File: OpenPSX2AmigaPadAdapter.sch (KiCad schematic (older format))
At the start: 47 parts, among them J1 TO_PSX_PAD, J2 DB9_F, J3 CONN_FTDI, J4 CONN_ICSP, J99 OSHW_LOGO, Q1 BSS138, Q2 BSS138, Q3 BSS138, Q4 BSS138, Q5 BSS138, U1 ATmega328P-AU, U2 TC1185-3.3V, U3 AD5242, Y1 16M, Y2 16M

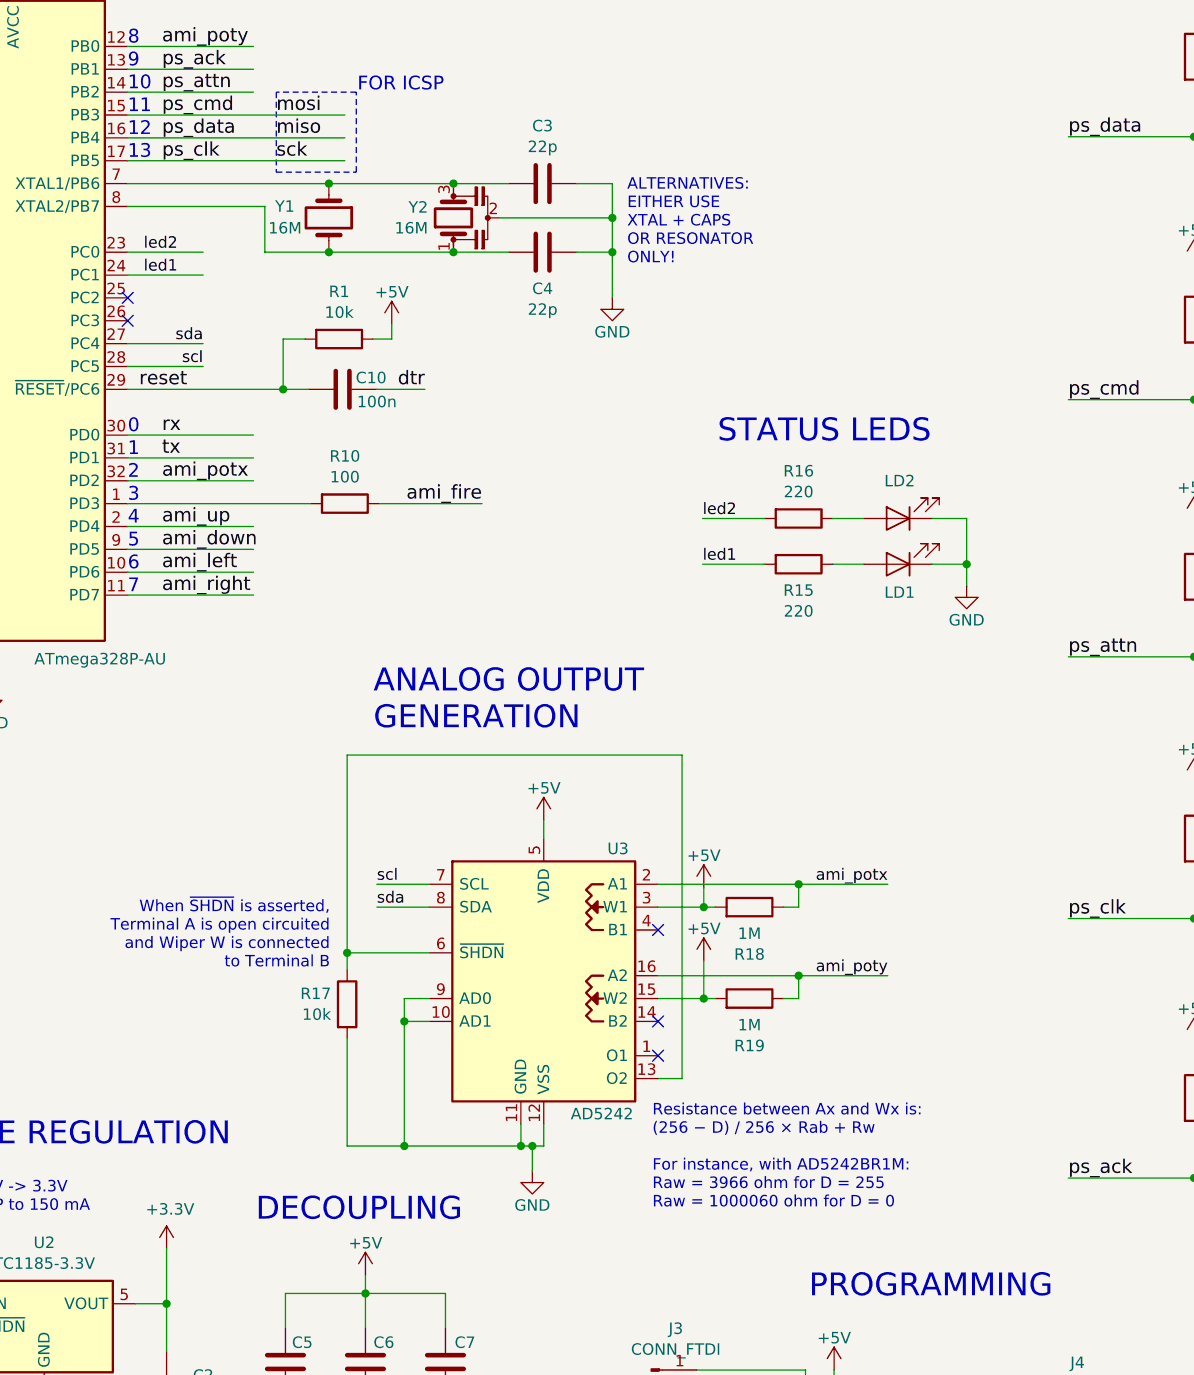
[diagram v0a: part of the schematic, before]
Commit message: PCB modifications for analog support are complete
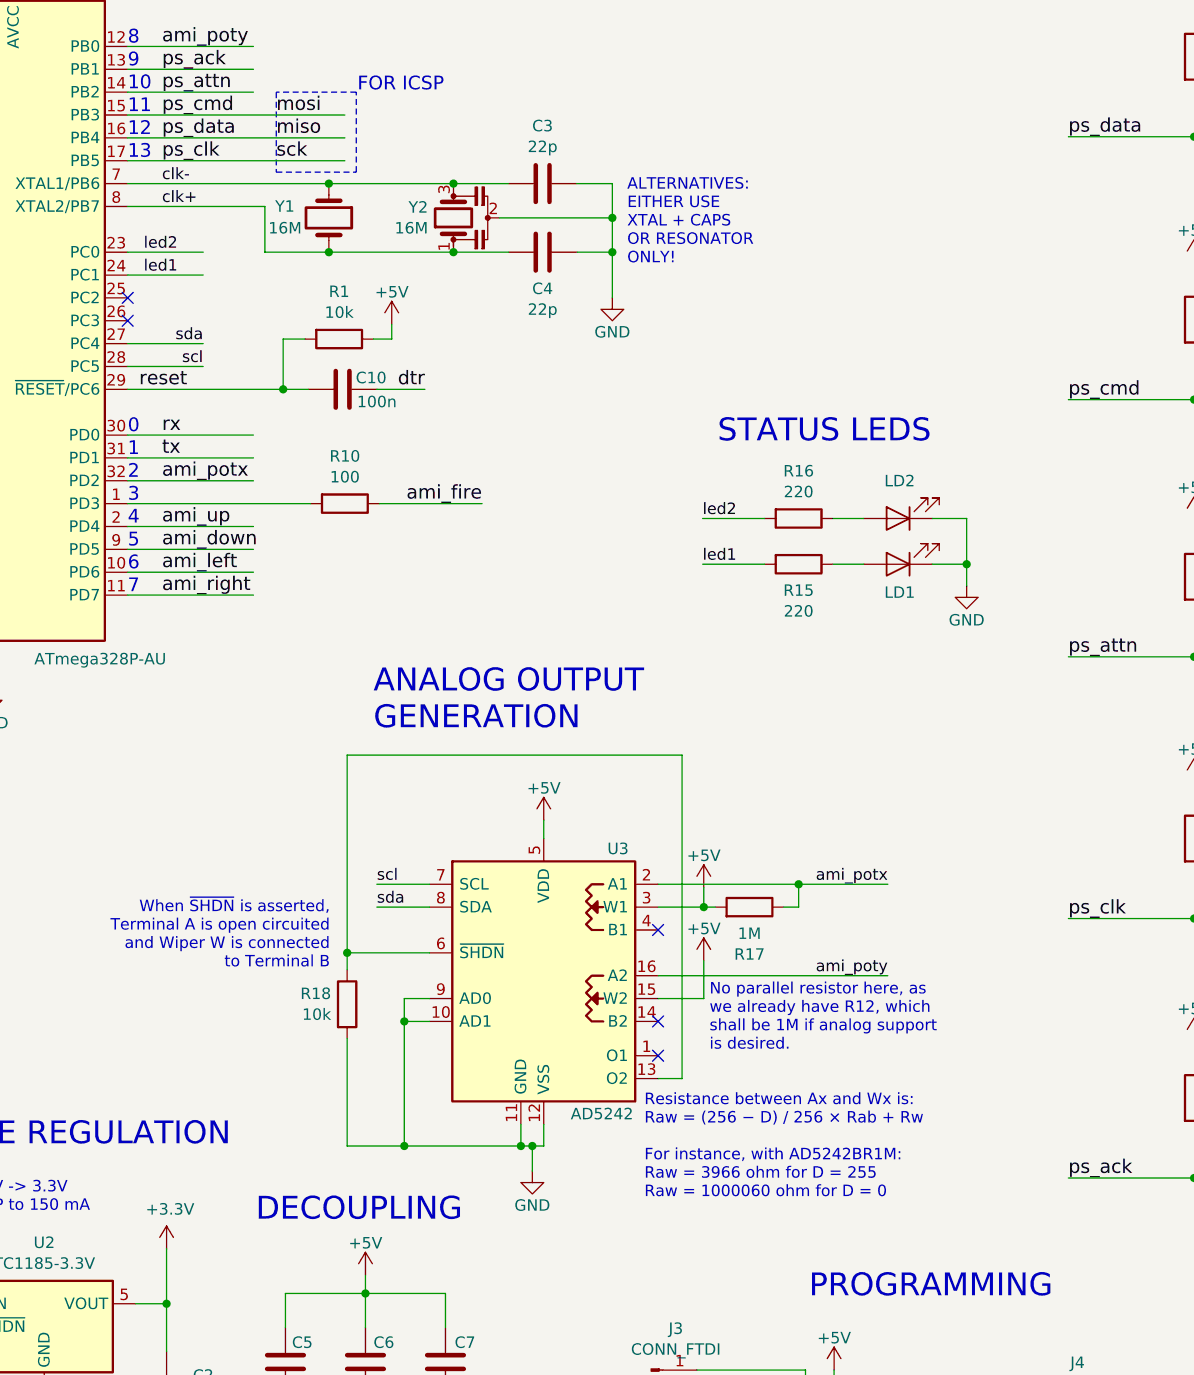
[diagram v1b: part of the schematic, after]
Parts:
- removed R19: 1M, Resistor_SMD:R_0805_2012Metric_Pad1.15x1.40mm_HandSolder, symbol Device:R
- renumbered R18 to R17, R17 to R18
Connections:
- net labels added: clk+, clk-
- wire segments 236 -> 232
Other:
- note added: "No parallel resistor here, as\nwe already have R12, which\nshall be 1M if analog support\nis desired."
- note added: "Resistance between Ax and Wx is:\nRaw = (256 − D) / 256 × Rab + Rw\n\nFor instance, with AD5242BR1M:\nRaw = 3966 ohm for D = 255\nRaw = 1000060 ohm for D = 0"
- note added: "When ~SHDN~ is asserted,\nTerminal A is open circuited\nand Wiper W is connected\nto Terminal B"
- note removed: "Resistance between Ax and Wx is:\n(256 − D) / 256 × Rab + Rw\n\nFor instance, with AD5242BR1M:\nRaw = 3966 ohm for D = 255\nRaw = 1000060 ohm for D = 0"
- note removed: "When ~SHDN is asserted,\nTerminal A is open circuited\nand Wiper W is connected\nto Terminal B"
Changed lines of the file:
@@
 P 2825 5430
 AR Path="/5EFED7F9/5F065439" Ref="R?"  Part="1"
-AR Path="/5F065439" Ref="R17"  Part="1"
-F 0 "R17" H 2755 5476 50  0000 R CNN
+AR Path="/5F065439" Ref="R18"  Part="1"
+F 0 "R18" H 2755 5476 50  0000 R CNN
 F 1 "10k" H 2755 5385 50  0000 R CNN
 F 2 "Resistor_SMD:R_0805_2012Metric_Pad1.15x1.40mm_HandSolder" V 2755 5430 50  0001 C CNN
@@
 P 4585 5005
 AR Path="/5EFED7F9/5F065454" Ref="R?"  Part="1"
-AR Path="/5F065454" Ref="R18"  Part="1"
-F 0 "R18" V 4378 5005 50  0000 C CNN
+AR Path="/5F065454" Ref="R17"  Part="1"
+F 0 "R17" V 4378 5005 50  0000 C CNN
 F 1 "1M" V 4469 5005 50  0000 C CNN
 F 2 "Resistor_SMD:R_0805_2012Metric_Pad1.15x1.40mm_HandSolder" V 4515 5005 50  0001 C CNN
@@
 Connection ~ 4385 5005
 Text Notes 2750 5280 2    50   ~ 0
-When ~SHDN is asserted,\nTerminal A is open circuited\nand Wiper W is connected\nto Terminal B
+When ~SHDN~ is asserted,\nTerminal A is open circuited\nand Wiper W is connected\nto Terminal B
 Wire Wire Line
 	4185 4905 4800 4905
@@
 Text Label 2195 2640 2    50   ~ 0
 scl
-Text Notes 4160 6330 0    50   ~ 0
-Resistance between Ax and Wx is:\n(256 − D) / 256 × Rab + Rw\n\nFor instance, with AD5242BR1M:\nRaw = 3966 ohm for D = 255\nRaw = 1000060 ohm for D = 0
 Wire Wire Line
 	4185 5405 4385 5405
@@
 Text Label 5190 5305 2    50   ~ 0
 ami_poty
-$Comp
-L Device:R R?
-U 1 1 5F06546B
-P 4585 5405
-AR Path="/5EFED7F9/5F06546B" Ref="R?"  Part="1"
-AR Path="/5F06546B" Ref="R19"  Part="1"
-F 0 "R19" V 4378 5405 50  0000 C CNN
-F 1 "1M" V 4469 5405 50  0000 C CNN
-F 2 "Resistor_SMD:R_0805_2012Metric_Pad1.15x1.40mm_HandSolder" V 4515 5405 50  0001 C CNN
-F 3 "~" H 4585 5405 50  0001 C CNN
-	1    4585 5405
-	0    1    -1   0
-$EndComp
-Connection ~ 4385 5405
-Wire Wire Line
-	4185 5305 4800 5305
-Wire Wire Line
-	4385 5405 4435 5405
-Wire Wire Line
-	4735 5405 4800 5405
-Wire Wire Line
-	4800 5405 4800 5305
-Connection ~ 4800 5305
-Wire Wire Line
-	4800 5305 5190 5305
 Wire Wire Line
 	4185 5755 4290 5755
 Wire Wire Line
 	4290 4340 4290 5755
+Text Notes 4125 6285 0    50   ~ 0
+Resistance between Ax and Wx is:\nRaw = (256 − D) / 256 × Rab + Rw\n\nFor instance, with AD5242BR1M:\nRaw = 3966 ohm for D = 255\nRaw = 1000060 ohm for D = 0
+Text Label 2015 1840 0    50   ~ 0
+clk-
+Text Label 2015 1940 0    50   ~ 0
+clk+
+Wire Wire Line
+	4185 5305 5190 5305
+Text Notes 4410 5640 0    50   ~ 0
+No parallel resistor here, as\nwe already have R12, which\nshall be 1M if analog support\nis desired.
 $EndSCHEMATC

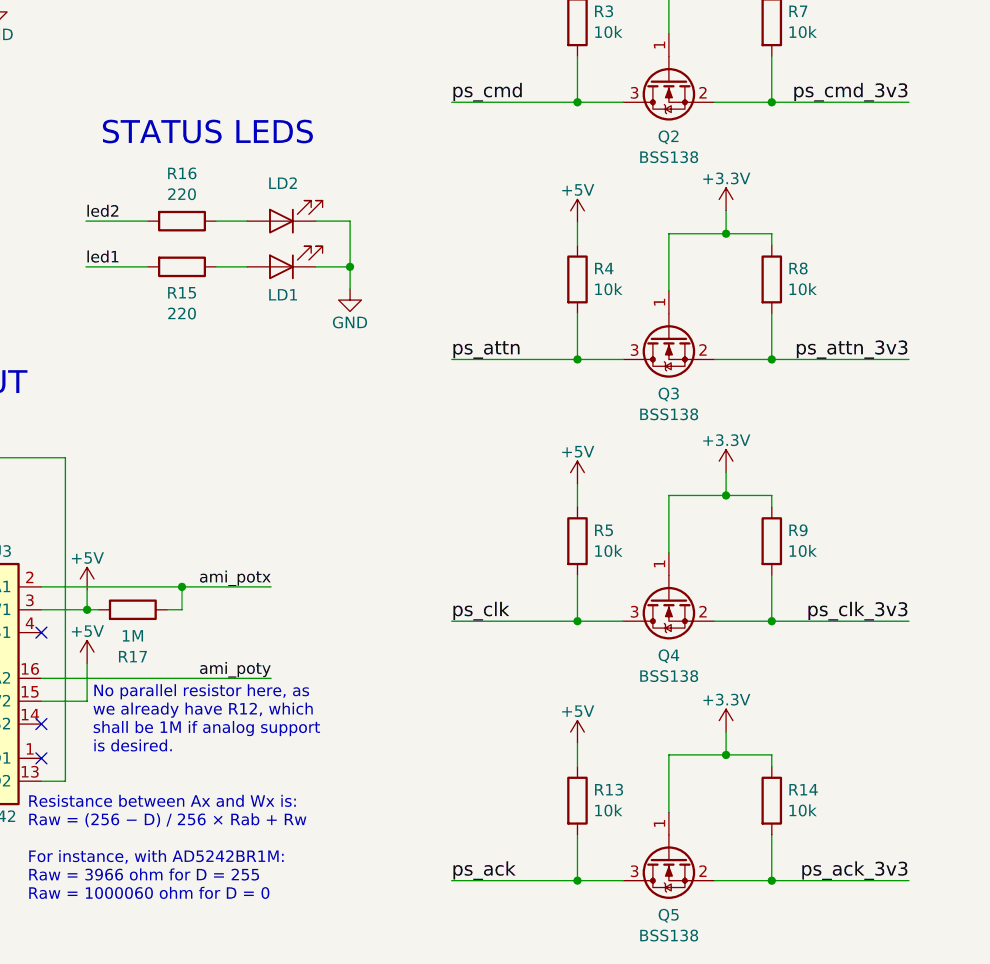
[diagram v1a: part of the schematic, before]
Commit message: Fix component naming
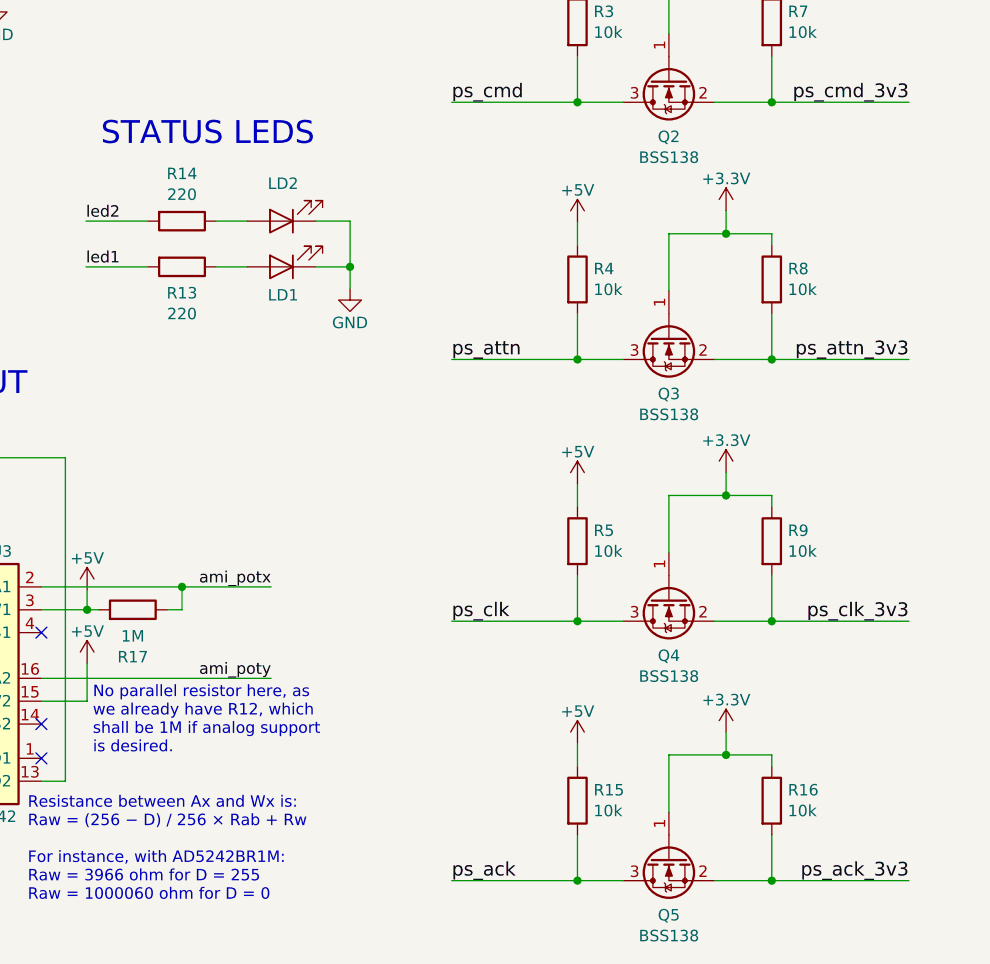
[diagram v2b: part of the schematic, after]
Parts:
- renumbered R15 to R13, R16 to R14, R13 to R15, R14 to R16
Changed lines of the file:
@@
 	5535 3505 5535 3600
 $Comp
-L Device:R R16
+L Device:R R14
 U 1 1 5D343268
 P 4800 3305
-F 0 "R16" V 4593 3305 50  0000 C CNN
+F 0 "R14" V 4593 3305 50  0000 C CNN
 F 1 "220" V 4684 3305 50  0000 C CNN
 F 2 "Resistor_SMD:R_0805_2012Metric_Pad1.15x1.40mm_HandSolder" V 4730 3305 50  0001 C CNN
@@
 $EndComp
 $Comp
-L Device:R R15
+L Device:R R13
 U 1 1 5D343E5C
 P 4800 3505
-F 0 "R15" V 4915 3505 50  0000 C CNN
+F 0 "R13" V 4915 3505 50  0000 C CNN
 F 1 "220" V 5006 3505 50  0000 C CNN
 F 2 "Resistor_SMD:R_0805_2012Metric_Pad1.15x1.40mm_HandSolder" V 4730 3505 50  0001 C CNN
@@
 	6530 6190 6730 6190
 $Comp
-L Device:R R13
+L Device:R R15
 U 1 1 5DFD8E76
 P 6530 5840
-F 0 "R13" H 6600 5886 50  0000 L CNN
+F 0 "R15" H 6600 5886 50  0000 L CNN
 F 1 "10k" H 6600 5795 50  0000 L CNN
 F 2 "Resistor_SMD:R_0805_2012Metric_Pad1.15x1.40mm_HandSolder" V 6460 5840 50  0001 C CNN
@@
 $EndComp
 $Comp
-L Device:R R14
+L Device:R R16
 U 1 1 5DFD8E80
 P 7380 5840
-F 0 "R14" H 7450 5886 50  0000 L CNN
+F 0 "R16" H 7450 5886 50  0000 L CNN
 F 1 "10k" H 7450 5795 50  0000 L CNN
 F 2 "Resistor_SMD:R_0805_2012Metric_Pad1.15x1.40mm_HandSolder" V 7310 5840 50  0001 C CNN

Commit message: Ready for V4
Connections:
- net labels added: dtr_in
- net labels removed: dtr
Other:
- note removed: "cts"
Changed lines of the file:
@@
 Title "OpenPSX2AmigaPadAdapter"
 Date "2020-03-26"
-Rev "4git"
+Rev "4"
 Comp "SukkoPera"
 Comment1 "Licensed under CERN OHL v.1.2"
@@
 Text Label 5370 7315 0    60   ~ 0
 sck
-Text Label 3165 2740 2    60   ~ 0
-dtr
+Text Label 3335 2740 2    60   ~ 0
+dtr_in
 Wire Wire Line
 	5770 7415 5370 7415
@@
 Text Label 4455 7430 0    60   ~ 0
 tx
-Text Label 4455 7530 0    60   ~ 0
-dtr
 $Comp
 L power:+5V #PWR025
@@
 $EndComp
 Wire Wire Line
-	2955 2740 3165 2740
+	2955 2740 3335 2740
 $Comp
 L Device:R R2
@@
 Wire Wire Line
 	4830 7130 4830 7290
-Text Notes 4455 7130 0    50   ~ 0
-cts
 Text Label 4455 7330 0    60   ~ 0
 rx
@@
 Text Notes 4410 5640 0    50   ~ 0
 No parallel resistor here, as\nwe already have R12, which\nshall be 1M if analog support\nis desired.
+Text Label 4455 7530 0    60   ~ 0
+dtr_in
 $EndSCHEMATC

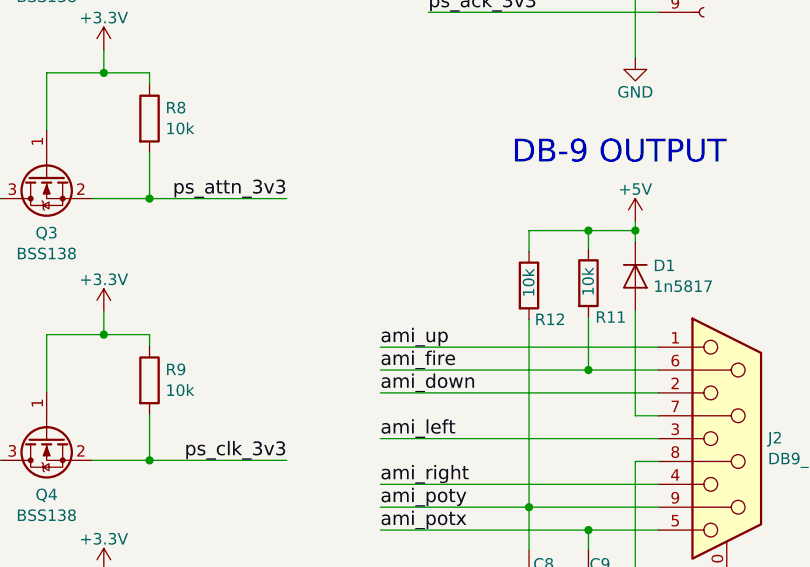
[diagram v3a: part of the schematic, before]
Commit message: Add note about R12
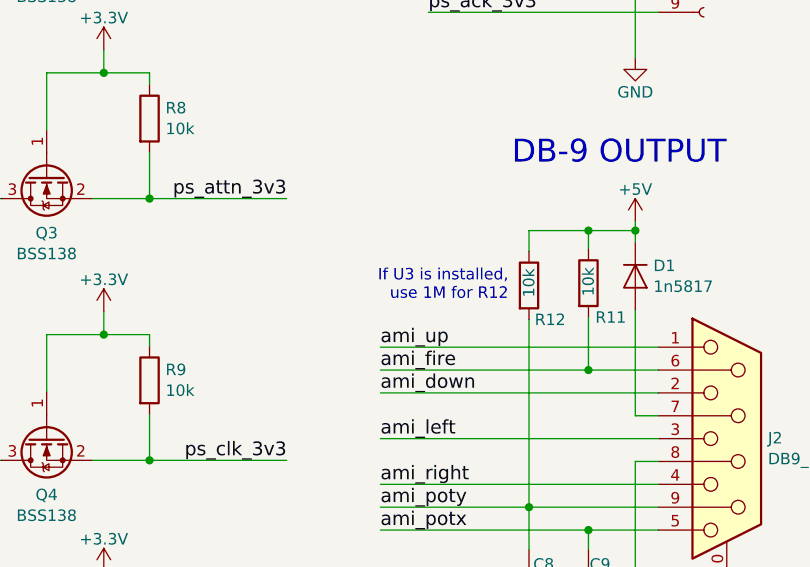
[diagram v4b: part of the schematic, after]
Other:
- note added: "If U3 is installed,\nuse 1M for R12"
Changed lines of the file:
@@
 Text Label 4455 7530 0    60   ~ 0
 dtr_in
+Text Notes 8950 4360 2    50   ~ 0
+If U3 is installed,\nuse 1M for R12
 $EndSCHEMATC
